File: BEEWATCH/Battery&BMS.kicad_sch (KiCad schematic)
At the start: 0 parts

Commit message: Inverted F Antenna designed
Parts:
- added C19, C21: 4.7uF, symbol Device:C_Small
- added C20: 1uF, symbol Device:C_Small
- added C22, C23: 0.1uF, symbol Device:C_Small
- added D1: LED, symbol Device:LED
- added D2: D_Schottky, symbol Device:D_Schottky
- added J2: BAT, symbol Connector_Generic:Conn_01x02
- added Q3: ~, Package_TO_SOT_SMD:SOT-23-3, symbol Project_Library:DMP1045U-7
- added R17, R19, R20: 22K, symbol Device:R_Small
- added R18: 220, symbol Device:R_Small
- added U5: MCP73832-2-OT, Package_TO_SOT_SMD:SOT-23-5, symbol Battery_Management:MCP73832-2-OT
- added U6, U7: XC6210B332MR, Package_TO_SOT_SMD:SOT-23-5, symbol Regulator_Linear:XC6210B332MR
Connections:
- new net: D1.1 (K), R18.2
- new net: R17.1, U5.5 (PROG)
- new net: R18.1, U5.1 (STAT)
- new net +3.3V: C22.1, U6.5 (VOUT)
- new net +5V: C21.1, D2.1 (K), Q3.2 (S), U6.1 (VIN), U6.3 (CE), U7.1 (VIN)
- new net 3V3: C23.1, U7.5 (VOUT)
- new net GND: C19.2, C20.2, C21.2, C22.2, C23.2, J2.2 (Pin_2), R17.2, R20.2, U5.2 (V_{SS}), U6.2 (GND), U7.2 (GND)
- new net PWR_EN: U7.3 (CE)
- new net PWR_SENSE: R19.2, R20.1
- new net VBAT: C19.1, J2.1 (Pin_1), Q3.3 (D), U5.3 (V_{BAT})
- new net VBUS: C20.1, D1.2 (A), D2.2 (A), Q3.1 (G), R19.1, U5.4 (V_{DD})
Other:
- note added: "IREG = 1000V ----- RPROG Where: RPROG = kOhms IREG = milliamper"

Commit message: Save Kicad files
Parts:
- renumbered C20 to C22, C19 to C23, C21 to C24, C22 to C25, C23 to C26, D2 to D1, D1 to D2, Q3 to Q2, R19 to R18, R18 to R19, R17 to R21

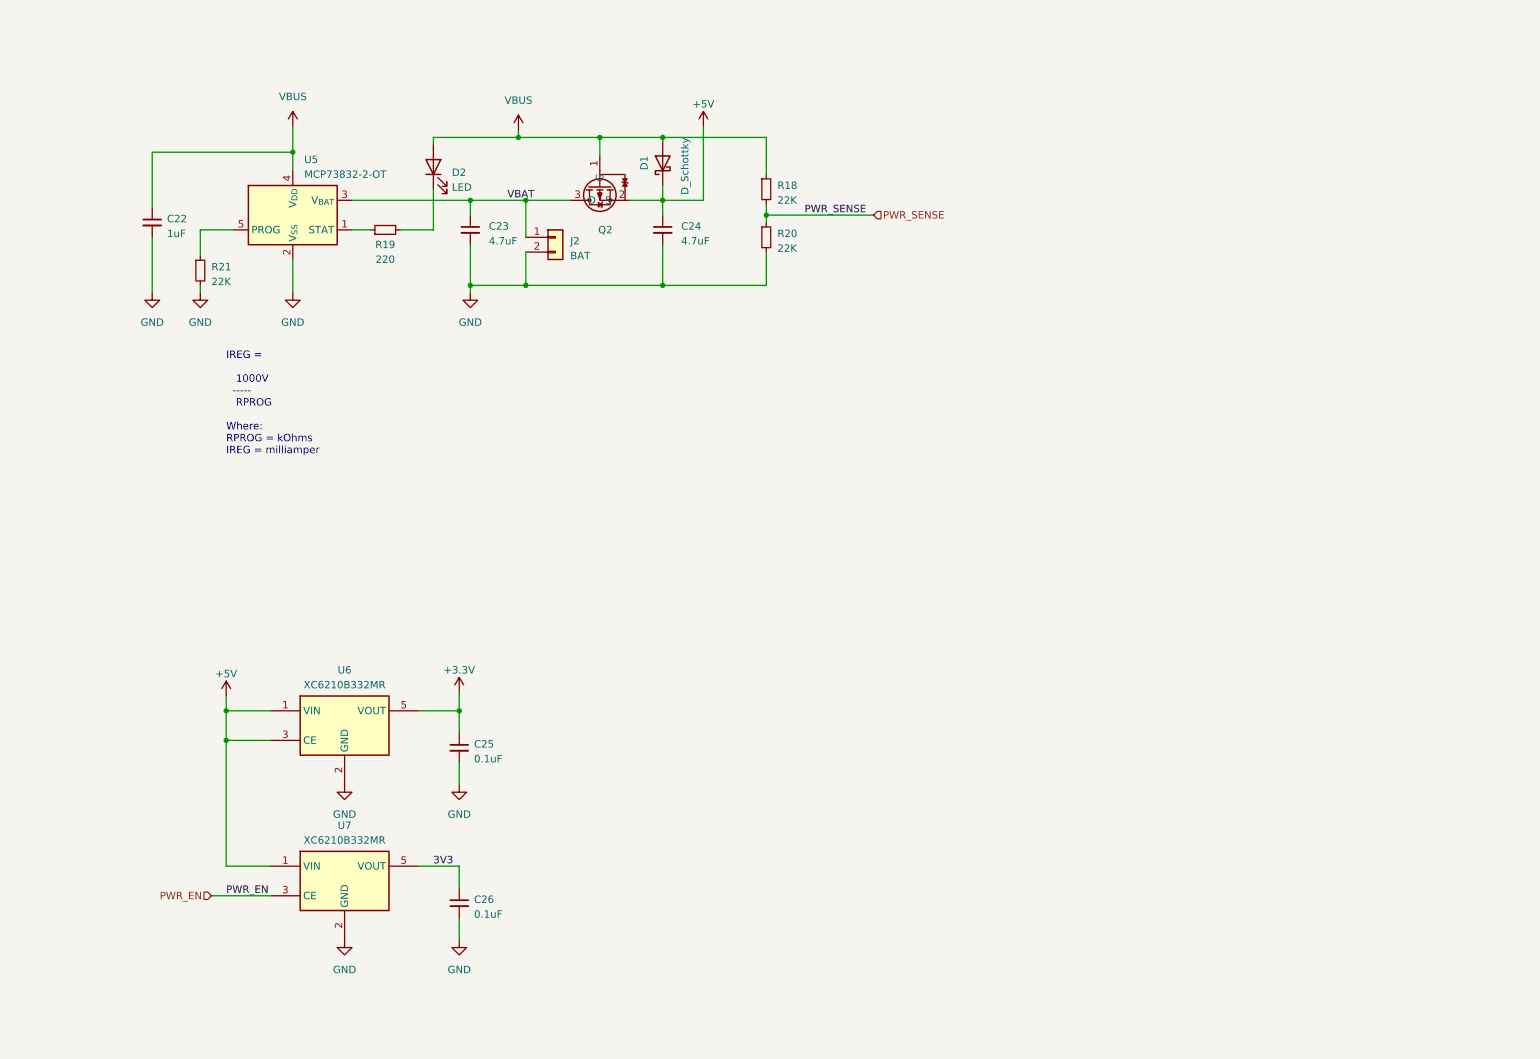
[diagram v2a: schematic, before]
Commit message: Insufficient GPIOs planning to add/C MUX or MCU
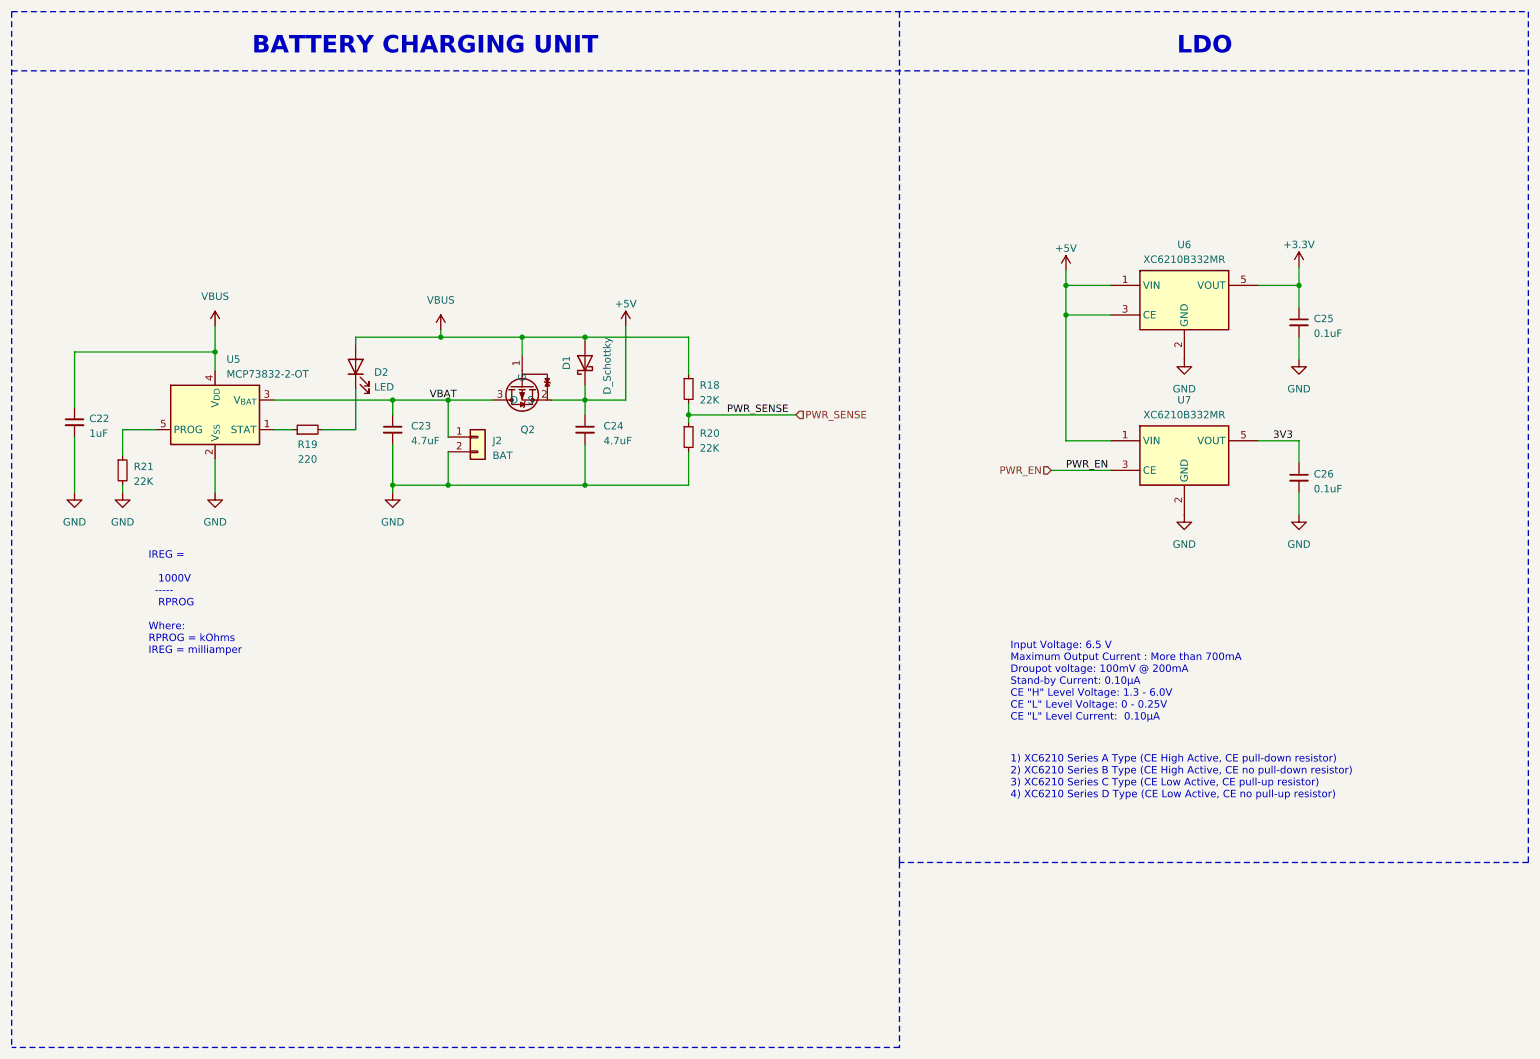
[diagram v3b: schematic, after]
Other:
- note added: "1) XC6210 Series A Type (CE High Active, CE pull-down resistor) 2) XC6210 Series B Type (CE High Active, CE no pull-down resistor) 3) XC6210 Series C Type (CE Low Active, CE pull-up resistor) 4) XC6210 Series D Type (CE Low Active, CE no pull-up resistor)"
- note added: "BATTERY CHARGING UNIT"
- note added: "Input Voltage: 6.5 V Maximum Output Current : More than 700mA Droupot voltage: 100mV @ 200mA Stand-by Current: 0.10μA CE "H" Level Voltage: 1.3 - 6.0V CE "L" Level Voltage: 0 - 0.25V CE "L" Level Current: 0.10μA"
- note added: "LDO"
- moved on the sheet: C22, C23, C24, C25, C26, D1, D2, J2, Q2, R18, R19, R20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
